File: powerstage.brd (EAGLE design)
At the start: 41.9 x 43.5 mm, 42 parts, among them CON1 PINHEAD_1X10-2-FEMALE, CON2 BATTERY_CON-2P-XT30-RA, CON3 PINHEAD_1X10-2-FEMALE, IC5 MCP9700, Q1 BUK9K6R2-40E,115, Q2 BUK9K6R2-40E,115, Q3 BUK9K6R2-40E,115

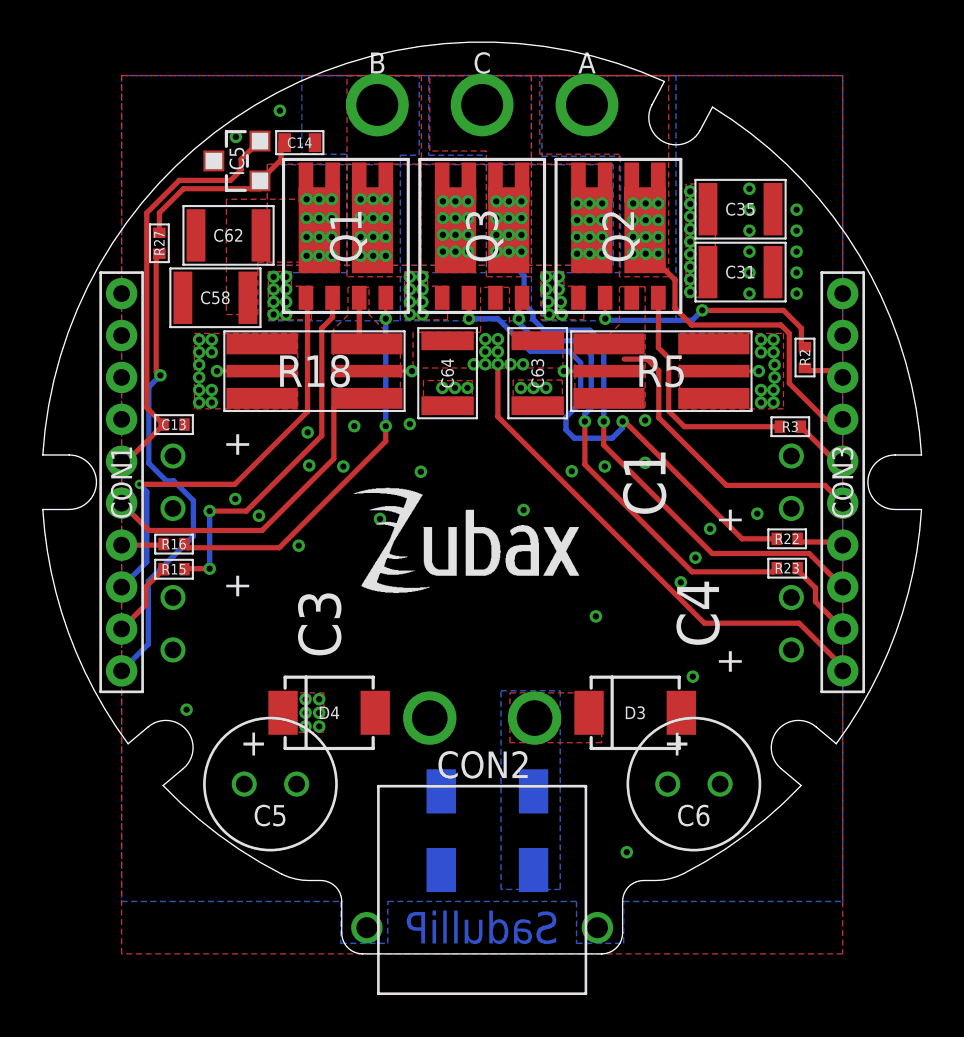
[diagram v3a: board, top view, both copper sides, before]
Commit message: fiducial marks
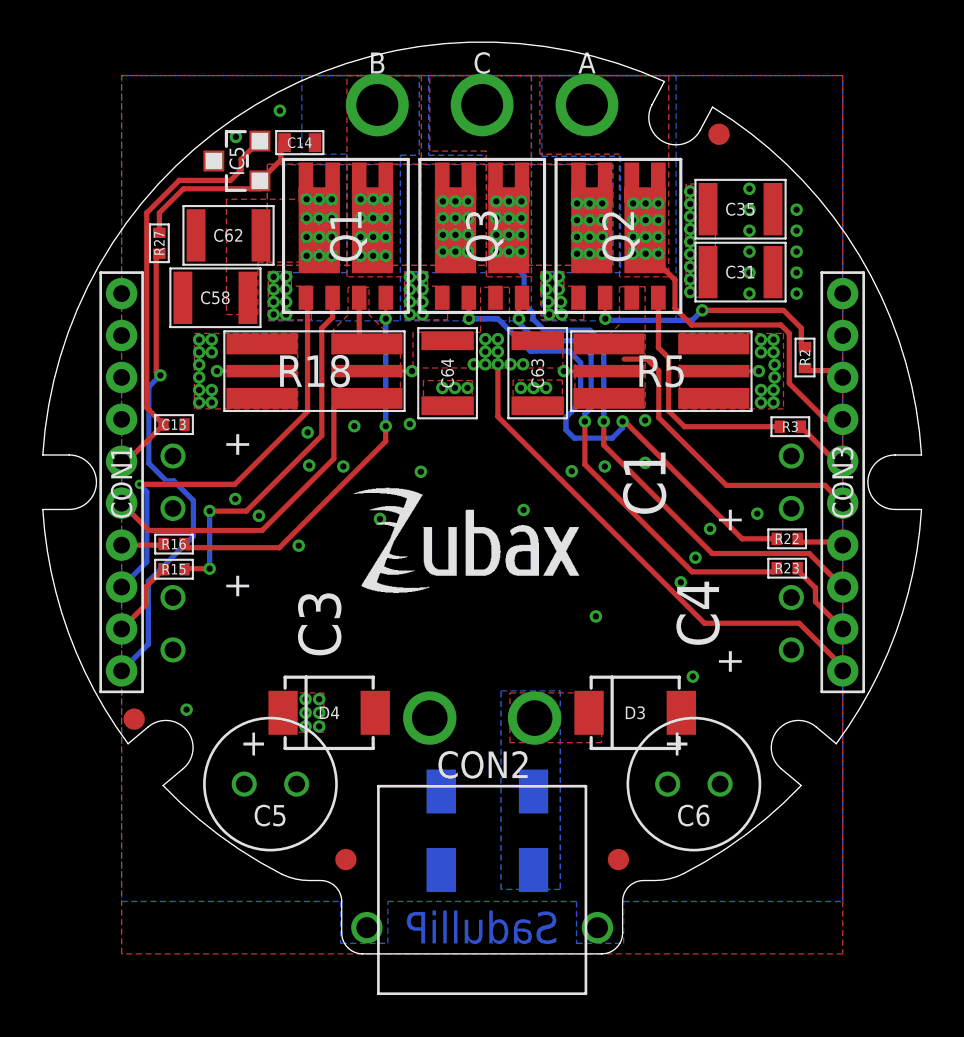
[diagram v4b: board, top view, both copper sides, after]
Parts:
- added U$10, U$12, U$8, U$9: FIDUCIALMOUNT, usb2can_master_lib:FIDUCIA-MOUNT
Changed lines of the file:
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@@
 <drawing>
 <settings>
-<setting alwaysvectorfont="yes"/>
+<setting alwaysvectorfont="no"/>
 <setting verticaltext="up"/>
 </settings>
 <grid distance="0.05" unitdist="mm" unit="mm" style="lines" multiple="1" display="yes" altdistance="5" altunitdist="mil" altunit="mil"/>
 <layers>
-<layer number="1" name="Top" color="4" fill="1" visible="no" active="yes"/>
+<layer number="1" name="Top" color="4" fill="1" visible="yes" active="yes"/>
 <layer number="2" name="Route2" color="43" fill="3" visible="no" active="yes"/>
 <layer number="3" name="Route3" color="17" fill="1" visible="no" active="no"/>
@@
 <layer number="14" name="Route14" color="22" fill="1" visible="no" active="no"/>
 <layer number="15" name="Route15" color="46" fill="6" visible="no" active="yes"/>
-<layer number="16" name="Bottom" color="1" fill="1" visible="yes" active="yes"/>
+<layer number="16" name="Bottom" color="1" fill="1" visible="no" active="yes"/>
 <layer number="17" name="Pads" color="2" fill="1" visible="yes" active="yes"/>
 <layer number="18" name="Vias" color="2" fill="1" visible="yes" active="yes"/>
 <layer number="19" name="Unrouted" color="6" fill="1" visible="yes" active="yes"/>
 <layer number="20" name="Dimension" color="24" fill="1" visible="yes" active="yes"/>
-<layer number="21" name="tPlace" color="7" fill="1" visible="no" active="yes"/>
-<layer number="22" name="bPlace" color="7" fill="1" visible="yes" active="yes"/>
-<layer number="23" name="tOrigins" color="15" fill="1" visible="no" active="yes"/>
-<layer number="24" name="bOrigins" color="15" fill="1" visible="yes" active="yes"/>
-<layer number="25" name="tNames" color="7" fill="1" visible="no" active="yes"/>
-<layer number="26" name="bNames" color="7" fill="1" visible="yes" active="yes"/>
+<layer number="21" name="tPlace" color="7" fill="1" visible="yes" active="yes"/>
+<layer number="22" name="bPlace" color="7" fill="1" visible="no" active="yes"/>
+<layer number="23" name="tOrigins" color="15" fill="1" visible="yes" active="yes"/>
+<layer number="24" name="bOrigins" color="15" fill="1" visible="no" active="yes"/>
+<layer number="25" name="tNames" color="7" fill="1" visible="yes" active="yes"/>
+<layer number="26" name="bNames" color="7" fill="1" visible="no" active="yes"/>
 <layer number="27" name="tValues" color="7" fill="1" visible="no" active="yes"/>
 <layer number="28" name="bValues" color="7" fill="1" visible="no" active="yes"/>
@@
 <layer number="49" name="Reference" color="7" fill="1" visible="no" active="yes"/>
 <layer number="50" name="dxf" color="7" fill="1" visible="no" active="yes"/>
-<layer number="51" name="tDocu" color="7" fill="1" visible="no" active="yes"/>
-<layer number="52" name="bDocu" color="7" fill="1" visible="yes" active="yes"/>
+<layer number="51" name="tDocu" color="7" fill="1" visible="yes" active="yes"/>
+<layer number="52" name="bDocu" color="7" fill="1" visible="no" active="yes"/>
 <layer number="53" name="tGND_GNDA" color="7" fill="9" visible="no" active="no"/>
 <layer number="54" name="bGND_GNDA" color="1" fill="9" visible="no" active="no"/>
@@
 </layers>
 <board>
-<fusionsync huburn="a.cGVyc29uYWw6dWUyYWE4ZDY4" projecturn="a.cGVyc29uYWw6dWUyYWE4ZDY4IzIwMTgxMTA4MTU5MTUwNTA2" f3durn="urn:adsk.wipprod:dm.lineage:PNkJALQsRiGXmceaXmEg1A" pcbguid="a30d68d2-795d-4aa0-9250-ee42eeb516a6" lastpulledtime="2018-11-12T11:47:08Z" lastsyncedchangeguid="465aaffa-2b27-a385-80e8-590b2e7f13d7"/>
+<fusionsync huburn="a.cGVyc29uYWw6dWUyYWE4ZDY4" projecturn="a.cGVyc29uYWw6dWUyYWE4ZDY4IzIwMTgxMTA4MTU5MTUwNTA2" f3durn="urn:adsk.wipprod:dm.lineage:erVD4M6GS8m25bkDTVKh3A" pcbguid="baa9c7f7-ef13-4156-bafc-bd75d4313cbc" lastpulledtime="" lastsyncedchangeguid="d71cca3a-fefb-157a-04fe-16d19bc77421"/>
 <plain>
 <wire x1="0" y1="0" x2="0" y2="21" width="0.1524" layer="49" style="shortdash" locked="yes"/>
@@
 </attributes>
 <variantdefs>
-<variantdef name="BASIC"/>
+<variantdef name="BASIC" current="yes"/>
 </variantdefs>
 <classes>
@@
 </autorouter>
 <elements>
-<element name="A" library="PADS" library_urn="urn:adsk.eagle:library:3188696" package="HOLE_2" package3d_urn="urn:adsk.eagle:package:4854323/1" value="PAD-HOLE_2" x="5" y="18" locked="yes" smashed="yes">
+<element name="A" library="PADS" library_urn="urn:adsk.eagle:library:3188696" package="HOLE_2" package3d_urn="urn:adsk.eagle:package:4854323/1" value="PAD-HOLE_2" x="5" y="18" locked="yes" populate="no" smashed="yes">
 <attribute name="BOM" value="EXCLUDE" x="5" y="18" size="1.778" layer="27" display="off"/>
 <attribute name="NAME" x="5" y="20" size="1" layer="25" font="vector" ratio="15" align="center"/>
@@
 <attribute name="VALUE" x="14.7" y="1.75" size="0.5" layer="27" font="vector" ratio="15" rot="R180" align="center"/>
 </element>
-<element name="B" library="PADS" library_urn="urn:adsk.eagle:library:3188696" package="HOLE_2" package3d_urn="urn:adsk.eagle:package:4854323/1" value="PAD-HOLE_2" x="-5" y="18" locked="yes" smashed="yes">
+<element name="B" library="PADS" library_urn="urn:adsk.eagle:library:3188696" package="HOLE_2" package3d_urn="urn:adsk.eagle:package:4854323/1" value="PAD-HOLE_2" x="-5" y="18" locked="yes" populate="no" smashed="yes">
 <attribute name="BOM" value="EXCLUDE" x="-5" y="18" size="1.778" layer="27" display="off"/>
 <attribute name="NAME" x="-5" y="20" size="1" layer="25" font="vector" ratio="15" align="center"/>
@@
 <attribute name="VALUE" x="-14.7" y="-2.05" size="0.5" layer="27" font="vector" ratio="15" align="center"/>
 </element>
-<element name="C" library="PADS" library_urn="urn:adsk.eagle:library:3188696" package="HOLE_2" package3d_urn="urn:adsk.eagle:package:4854323/1" value="PAD-HOLE_2" x="0" y="18" locked="yes" smashed="yes">
+<element name="C" library="PADS" library_urn="urn:adsk.eagle:library:3188696" package="HOLE_2" package3d_urn="urn:adsk.eagle:package:4854323/1" value="PAD-HOLE_2" x="0" y="18" locked="yes" populate="no" smashed="yes">
 <attribute name="BOM" value="EXCLUDE" x="0" y="18" size="1.778" layer="27" display="off"/>
 <attribute name="NAME" x="0" y="20" size="1" layer="25" font="vector" ratio="15" align="center"/>
@@
 <attribute name="VALUE" x="14.55" y="-5" size="0.5" layer="27" font="vector" ratio="15" rot="R180" align="center"/>
 </element>
-<element name="S1" library="misc" library_urn="urn:adsk.eagle:library:5347860" package="SENSE-0.6" value="SENSE" x="0.75" y="5.625" smashed="yes" rot="R90">
+<element name="S1" library="misc" library_urn="urn:adsk.eagle:library:5347860" package="SENSE-0.6" value="SENSE" x="0.75" y="5.625" populate="no" smashed="yes" rot="R90">
 <attribute name="BOM" value="EXCLUDE" x="63.75" y="-20.375" size="1.778" layer="27" rot="R90" display="off"/>
 </element>
@@
 <element name="U$2" library="logo" library_urn="urn:adsk.eagle:library:6668987" package="DUCK-8.5X7.5-MASK" value="" x="-4.5" y="-22.475" smashed="yes"/>
 <element name="U$4" library="logo" library_urn="urn:adsk.eagle:library:6668987" package="OSHW-10.5X11.5" value="" x="5.475" y="-8.525" smashed="yes" rot="MR0"/>
+<element name="U$8" library="usb2can_master_lib" package="FIDUCIA-MOUNT" value="FIDUCIALMOUNT" x="-6.5" y="-18" populate="no" smashed="yes"/>
+<element name="U$9" library="usb2can_master_lib" package="FIDUCIA-MOUNT" value="FIDUCIALMOUNT" x="6.5" y="-18" populate="no" smashed="yes"/>
+<element name="U$10" library="usb2can_master_lib" package="FIDUCIA-MOUNT" value="FIDUCIALMOUNT" x="11.3" y="16.6" populate="no" smashed="yes"/>
+<element name="U$12" library="usb2can_master_lib" package="FIDUCIA-MOUNT" value="FIDUCIALMOUNT" x="-16.6" y="-11.3" populate="no" smashed="yes"/>
 </elements>
 <signals>
@@
 <wire x1="16.35" y1="-0.15" x2="17.2" y2="-1" width="0.25" layer="1"/>
 <wire x1="11.65" y1="-0.15" x2="16.35" y2="-0.15" width="0.25" layer="1"/>
-<wire x1="6.05" y1="4" x2="6.775" y2="5.875" width="0" layer="19" extent="1-1"/>
+<wire x1="6.775" y1="5.875" x2="6.05" y2="4" width="0" layer="19" extent="1-1"/>
 </signal>
 <signal name="PHASE_A" class="1">
@@
 <via x="5.425" y="-6.4" extent="1-16" drill="0.3" diameter="0.6"/>
 <via x="-14.1" y="-10.85" extent="1-16" drill="0.3" diameter="0.6"/>
-<via x="6.9" y="-17.65" extent="1-16" drill="0.3" diameter="0.6"/>
 <via x="10.05" y="-9.275" extent="1-16" drill="0.3" diameter="0.6"/>
 <via x="1.975" y="-1.325" extent="1-16" drill="0.3" diameter="0.6"/>
